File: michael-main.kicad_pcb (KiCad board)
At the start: 4 copper layers, 98 x 119.8 mm, 179 parts, among them J1 Conn_01x03_Pin, J14 Conn_01x02_Pin, J15 Conn_01x02_Pin, J17 Conn_01x03_Pin, J18 Conn_01x05_Pin, J19 Conn_01x03_Pin, J2 PPTC041LGBN-RC, J21 Conn_01x05_Pin, J22 Conn_01x02_Pin, J25 Conn_01x09_Socket, J27 Conn_01x07_Socket, J28 XT30PW_2_2_-M.G.B, J29 XT30PW_2_2_-M.G.B, J3 Conn_01x03_Pin, J30 XT30PW_2_2_-M.G.B, J31 XT30PW_2_2_-M.G.B, J4 Conn_01x05_Pin, J5 Conn_01x05_Pin, J7 Conn_01x03_Pin, J8 USB_B_Mini, J9 Conn_01x05_Pin, Q1 BSC340N08NS3G, Q2 BSC340N08NS3G, Q3 BSC340N08NS3G, Q4 BSC340N08NS3G, U1 STM32F446RETx, U11 LMR14050SDDAR, U12 LMR14050SDDAR, U13 STM32F446RETx, U14 LM1084-5.0, U16 LM1084-3.3, U17 SN65HVD230, U18 SN65HVD230, U2 SN65HVD230, U3 STM32F446RETx, U4 SN65HVD230, U5 USBLC6-4SC6, U6 STM32F446RETx, U8 LTC7000EMSE-1_TRPBF, U9 STM32F446RETx, Y1 Crystal, Y2 8Mhz, Y3 Crystal, Y4 Crystal, Y5 Crystal

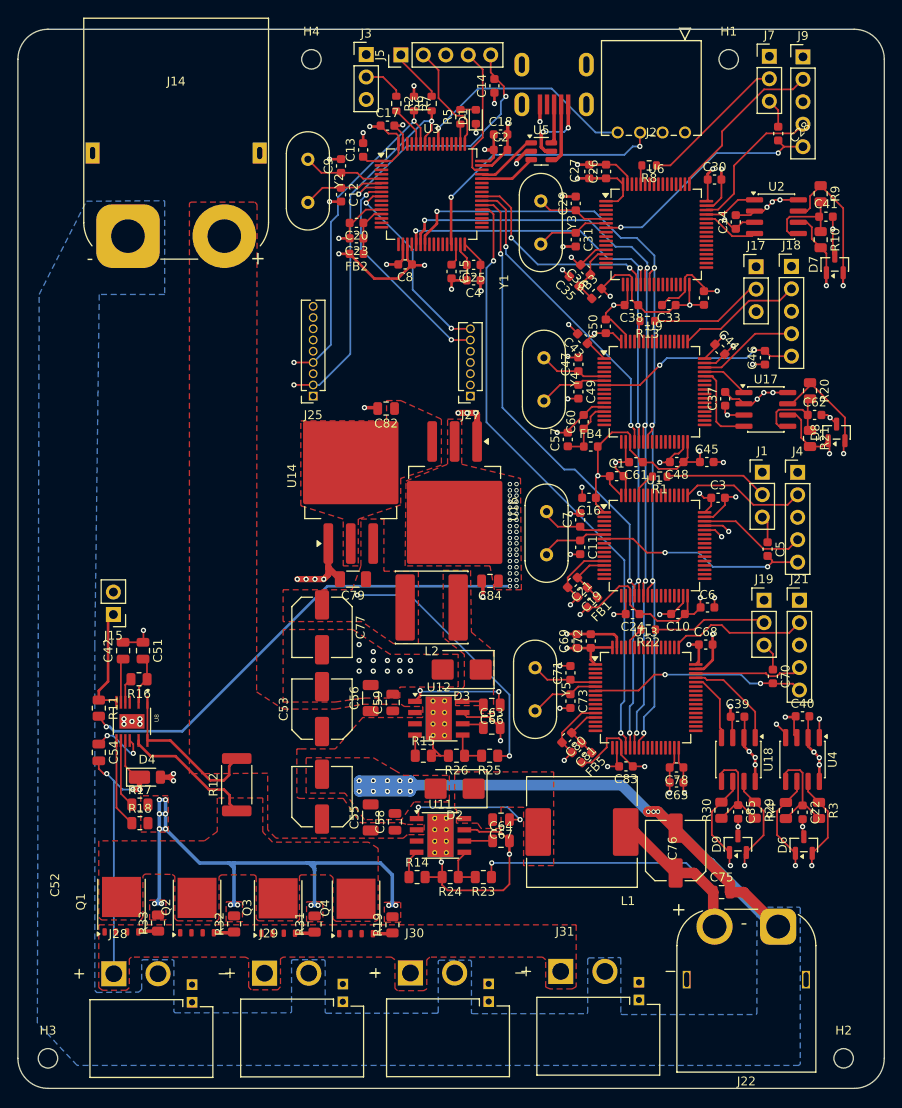
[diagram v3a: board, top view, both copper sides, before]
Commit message: finished solder mask removal, switched to a smaller crystal, finished osc signal isolation
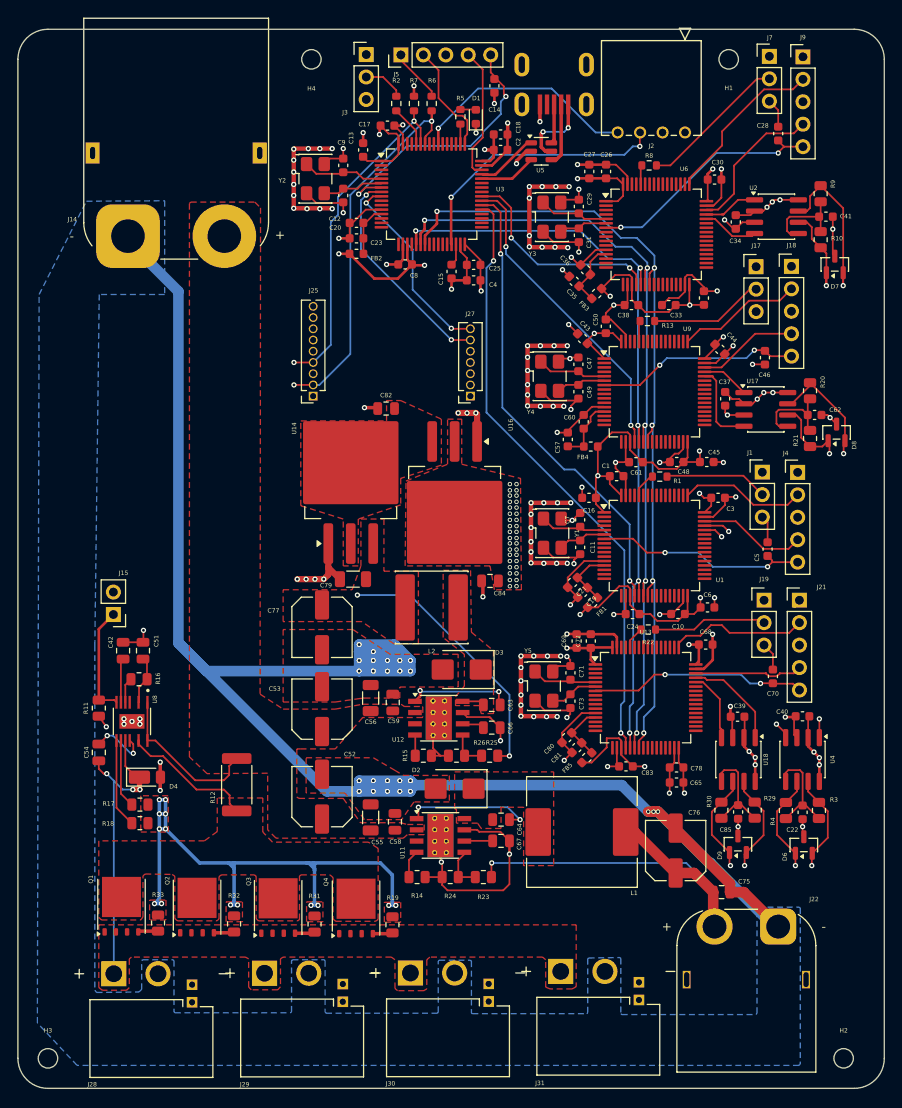
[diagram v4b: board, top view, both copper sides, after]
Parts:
- Y1, Y2, Y3, Y4, Y5: footprint Crystal:Crystal_HC49-U_Vertical -> Crystal:Crystal_SMD_5032-4Pin_5.0x3.2mm
- moved Y1 2.53 mm to (97.0, 105.6)
- moved Y2 2.35 mm to (70.2, 65.5)
- moved Y5 2.31 mm to (96.1, 122.9)
- moved Y3 2.22 mm to (97.0, 69.8)
- moved Y4 2.19 mm to (96.8, 87.8)
- moved C31 0.61 mm to (100.0, 71.9)
- moved C29 0.49 mm to (100.0, 68.7)
- moved C12 0.27 mm to (73.4, 67.4)
- moved C9 0.26 mm to (73.4, 64.0)
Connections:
- Y1 pad 2: Net-(U1-PH1) -> GND
- Y2 pad 2: Net-(U3-PH1) -> GND
- Y3 pad 2: Net-(U6-PH1) -> GND
- Y4 pad 2: Net-(U9-PH1) -> GND
- Y5 pad 2: Net-(U13-PH1) -> GND
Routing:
- net GND: track 367.9 -> 603.5 mm, vias 106 -> 164
- net Net-(U6-PH1): track 8.35 -> 5.69 mm
- net Net-(U13-PH1): track 7.96 -> 5.49 mm
- net Net-(U3-PH1): track 9.23 -> 7.00 mm
- net Net-(U9-PH1): track 7.77 -> 5.71 mm
- net Net-(U1-PH1): track 7.31 -> 5.50 mm

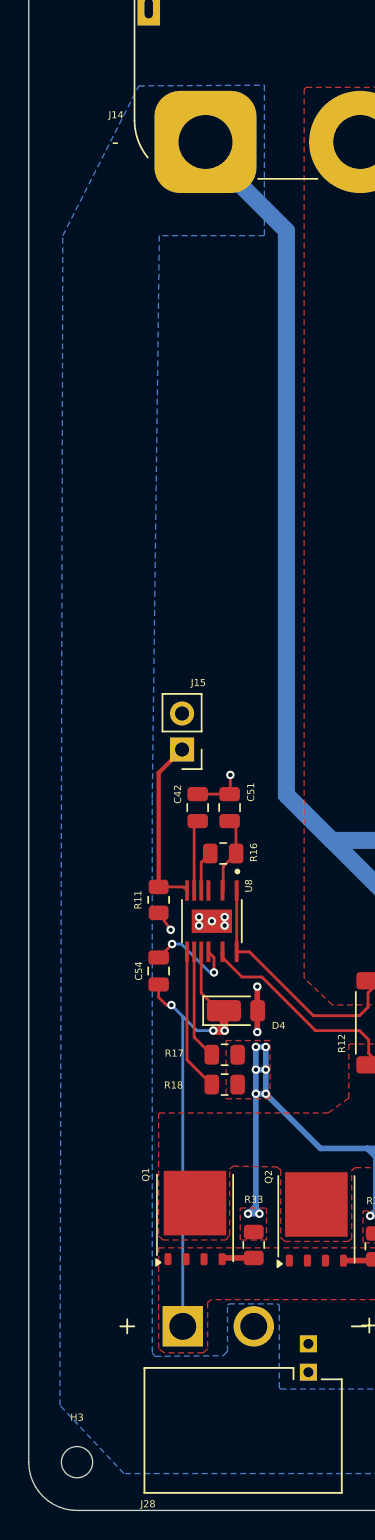
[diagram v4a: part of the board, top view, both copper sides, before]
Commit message: exposed back plate gnd trace
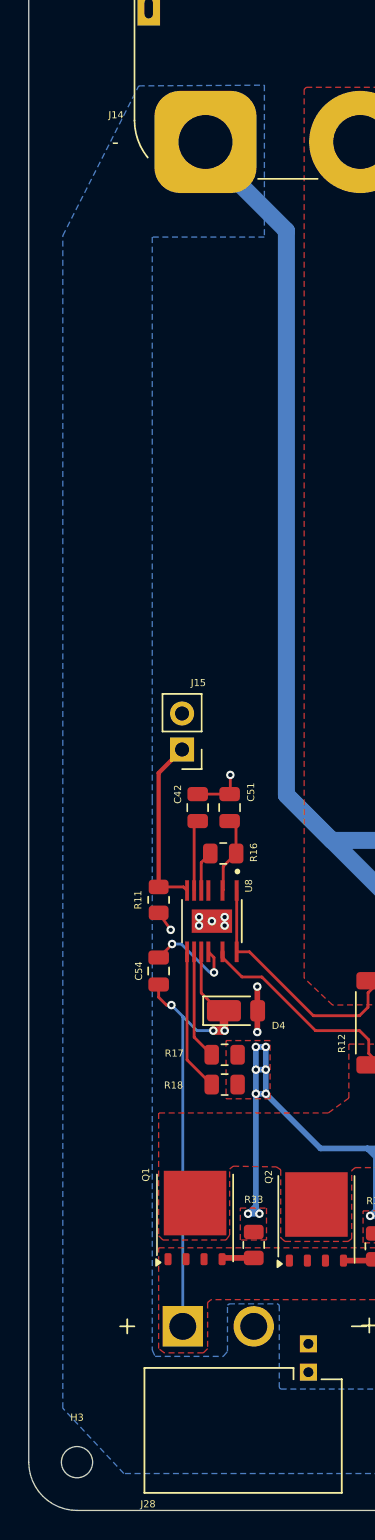
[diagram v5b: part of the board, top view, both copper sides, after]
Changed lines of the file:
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@@
 				(xy 101.05 159.85) (xy 101.05 153.75) (xy 101.15 153.65) (xy 104.7 153.6) (xy 104.8 153.7) (xy 104.8 159.95)
 				(xy 104.9 160.05) (xy 120.1 160.05) (xy 120.2 159.9) (xy 120.2 148) (xy 120.3 147.9) (xy 125 147.9)
-				(xy 125.1 148) (xy 125.1 165.65) (xy 124.95 165.8) (xy 43.3 165.8) (xy 38.8 161) (xy 39 78.6) (xy 44.35 68.05)
-				(xy 53.2 68) (xy 53.2 78.6) (xy 45.8 78.6) (xy 45.3 118.3) (xy 45.3 157.3) (xy 45.5 157.55) (xy 50.3 157.5)
+				(xy 125.1 148) (xy 125.1 165.65) (xy 124.95 165.8) (xy 43.3 165.8) (xy 39 161.2) (xy 39 78.6) (xy 44.35 68.05)
+				(xy 53.2 68) (xy 53.2 78.7) (xy 45.3 78.7) (xy 45.3 118.3) (xy 45.3 157.1) (xy 45.5 157.55) (xy 50.3 157.55)
 			)
 		)
+	)
+	(zone
+		(net 0)
+		(net_name "")
+		(layer "B.Mask")
+		(hatch edge 0.5)
+		(connect_pads
+			(clearance 0.5)
+		)
+		(min_thickness 0.25)
+		(filled_areas_thickness no)
+		(fill yes
+			(thermal_gap 0.5)
+			(thermal_bridge_width 0.5)
+		)
+		(polygon
+			(pts
+				(xy 45.2 78.7) (xy 45.2 157.1) (xy 45.4 157.6) (xy 50.7 157.6) (xy 50.7 155.5) (xy 54.1 155.5) (xy 54.1 160)
+				(xy 67.6 160) (xy 67.6 155.5) (xy 71.3 155.5) (xy 71.3 160) (xy 84.2 160) (xy 84.2 155.4) (xy 87.8 155.4)
+				(xy 87.8 160) (xy 101.2 160) (xy 101.2 155.1) (xy 104.7 155.1) (xy 104.7 165.7) (xy 43.4 165.7)
+				(xy 39.1 161.1) (xy 39.1 78.6) (xy 44.4 68.1) (xy 52.6 68.1) (xy 52.6 78.7)
+			)
+		)

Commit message: edited master mcu section
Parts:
- removed J2: PPTC041LGBN-RC, pptc041lgbn-rc:CONN_PPTC041LGBN-RC_SUL
- R12: value 1m -> 0.5m
- U14, U16: footprint Package_TO_SOT_SMD:TO-263-3_TabPin4 -> Package_TO_SOT_SMD:TO-263-3_TabPin2
- Y1, Y2, Y3, Y4, Y5: footprint Crystal:Crystal_SMD_5032-4Pin_5.0x3.2mm -> Crystal:Crystal_HC49-U_Vertical
- moved C34 20.2 mm to (124.3, 51.3), turned to 0 degrees
- moved J7 17.0 mm to (105.0, 55.4)
- moved J9 16.7 mm to (108.7, 51.6), turned to 90 degrees
- moved U2 13.9 mm to (124.2, 56.0), turned to -90 degrees
- moved H1 13.0 mm to (130.0, 52.0)
- moved R10 11.6 mm to (122.1, 62.1), turned to 90 degrees
- moved D7 10.3 mm to (124.1, 66.1)
- moved C41 8.43 mm to (124.1, 62.3), turned to -90 degrees
- moved C28 6.21 mm to (119.2, 55.2), turned to 180 degrees
- moved R9 5.24 mm to (126.1, 62.1)
- moved Y2 2.43 mm to (69.6, 63.2)
- moved J14 2.10 mm to (49.0, 74.1)
- moved C8 0.76 mm to (80.1, 75.9), turned to 90 degrees
- moved H4 0.20 mm to (70.0, 52.0)
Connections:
- U3 pad 29: /Screen_SCL -> unconnected-(U3-PB10-Pad29)
- U3 pad 55: /Screen_SDA -> unconnected-(U3-PB3-Pad55)
- Y1 pad 2: GND -> Net-(U1-PH1)
- Y2 pad 2: GND -> Net-(U3-PH1)
- Y3 pad 2: GND -> Net-(U6-PH1)
- Y4 pad 2: GND -> Net-(U9-PH1)
- Y5 pad 2: GND -> Net-(U13-PH1)
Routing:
- net GND: track 603.5 -> 507.6 mm, vias 164 -> 110
- net /Screen_SCL: track 30.7 -> 0.00 mm, vias 2 -> 0
- net /Screen_SDA: track 26.0 -> 0.00 mm, vias 1 -> 0
- net Net-(J7-Pin_2): track 16.4 -> 7.64 mm
- net /CANH2: track 143.7 -> 137.1 mm
- net /NRST: track 30.6 -> 25.9 mm
- net /TCK2: track 19.7 -> 15.7 mm
- net /NRST2: track 27.0 -> 30.4 mm
- net /TMS2: track 16.9 -> 19.8 mm
- net /Vref2_CAN: track 9.98 -> 12.8 mm
- net /CAN2_TX: track 6.34 -> 9.12 mm
- net /INT2: track 22.4 -> 19.8 mm, vias 2 -> 1
- net +3.3V: track 238.0 -> 235.5 mm
- net /SCK_SCL: track 43.7 -> 41.3 mm, vias 2 -> 1
- net /SDI_SDA: track 38.3 -> 36.1 mm, vias 2 -> 1
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
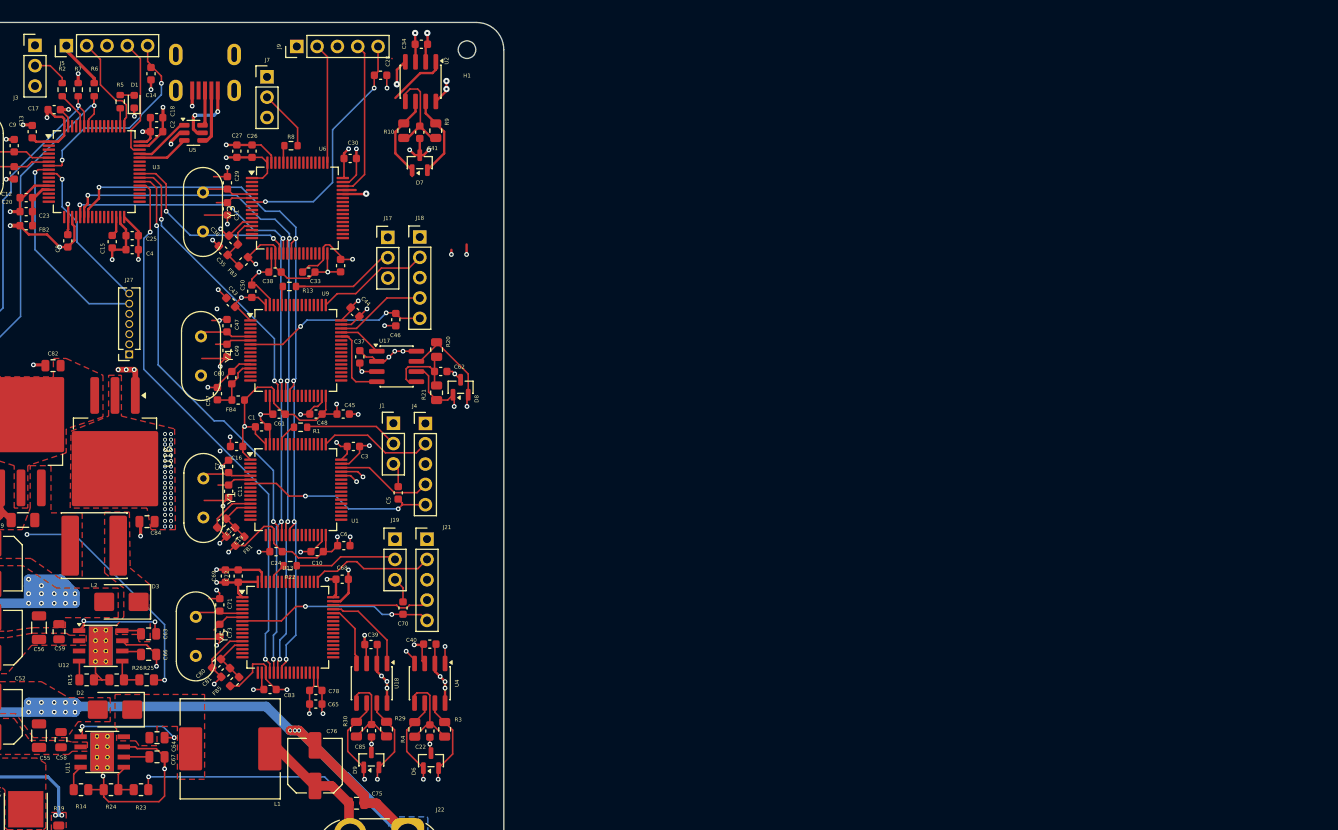
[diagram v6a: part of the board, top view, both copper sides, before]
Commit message: refined slave mcu section
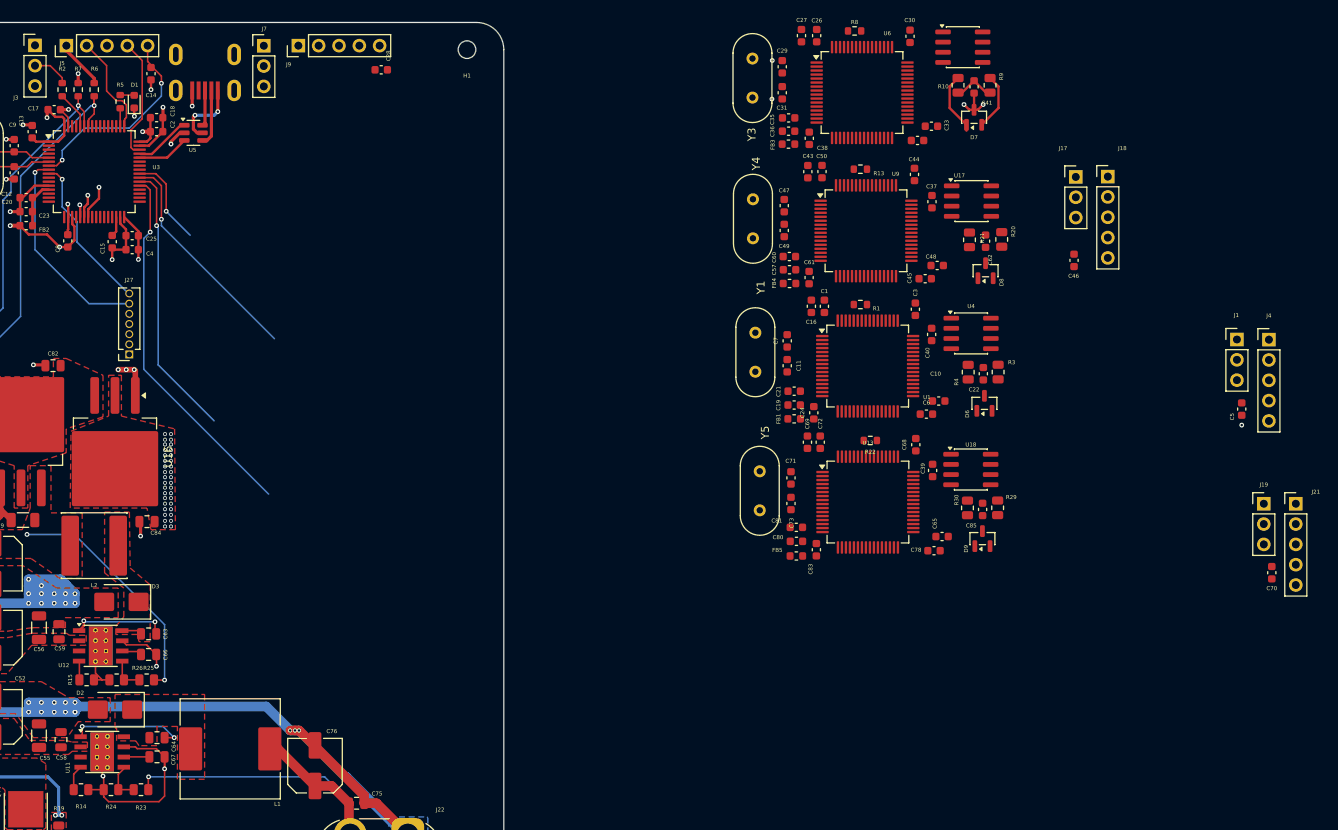
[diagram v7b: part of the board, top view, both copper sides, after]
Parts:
- removed C34: 0.1uF, Capacitor_SMD:C_0603_1608Metric
- moved C70 108.7 mm to (230.6, 117.4)
- moved J19 108.7 mm to (229.6, 108.8)
- moved J21 108.7 mm to (233.6, 108.8)
- moved J1 106.0 mm to (226.2, 88.2)
- moved J4 106.0 mm to (230.2, 88.2)
- moved C5 106.0 mm to (226.8, 96.9)
- moved J17 86.3 mm to (206.1, 67.9)
- moved J18 86.3 mm to (210.1, 67.9)
- moved C46 85.1 mm to (205.9, 78.3)
- moved D6 82.3 mm to (194.7, 96.2)
- moved R4 82.3 mm to (192.6, 92.3)
- moved C22 82.3 mm to (194.5, 92.5)
- moved R3 82.3 mm to (196.4, 92.3)
- moved D9 81.2 mm to (194.4, 113.1)
- moved R29 81.2 mm to (196.3, 109.3)
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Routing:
- net GND: track 507.6 -> 317.7 mm, vias 110 -> 62
- net +3.3V: track 235.5 -> 93.6 mm, vias 61 -> 42
- net /SPI_MOSI: track 93.7 -> 4.28 mm, vias 5 -> 1
- net /SPI_MISO: track 91.3 -> 2.91 mm, vias 5 -> 1
- net /SPI_SCK: track 89.1 -> 1.55 mm, vias 5 -> 1
- net /CANH2: track 137.1 -> 54.6 mm, vias 1 -> 0
- net /CANL2: track 135.4 -> 53.9 mm, vias 1 -> 0
- net /CANH3: track 93.0 -> 27.8 mm, vias 1 -> 0
- net /CANL3: track 86.9 -> 26.3 mm, vias 1 -> 0
- net /CAN1_TX: track 31.9 -> 0.00 mm, vias 2 -> 0
- net /NRST2: track 30.4 -> 0.00 mm, vias 2 -> 0
- net /CAN1_RX: track 28.0 -> 0.00 mm, vias 2 -> 0
- net /NRST4: track 24.6 -> 0.00 mm, vias 2 -> 0
- net /NRST1: track 24.3 -> 0.00 mm, vias 2 -> 1
- net /NRST3: track 23.1 -> 0.00 mm, vias 2 -> 0
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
